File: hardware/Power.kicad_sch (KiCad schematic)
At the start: 22 parts, among them J1 BarrelJack, Q1 DMP3099L-7, U1 ADP7142AUJZ-3.3, U2 ADP7142AUJZ-5.0, U3 ADP7142AUJZ-2.5

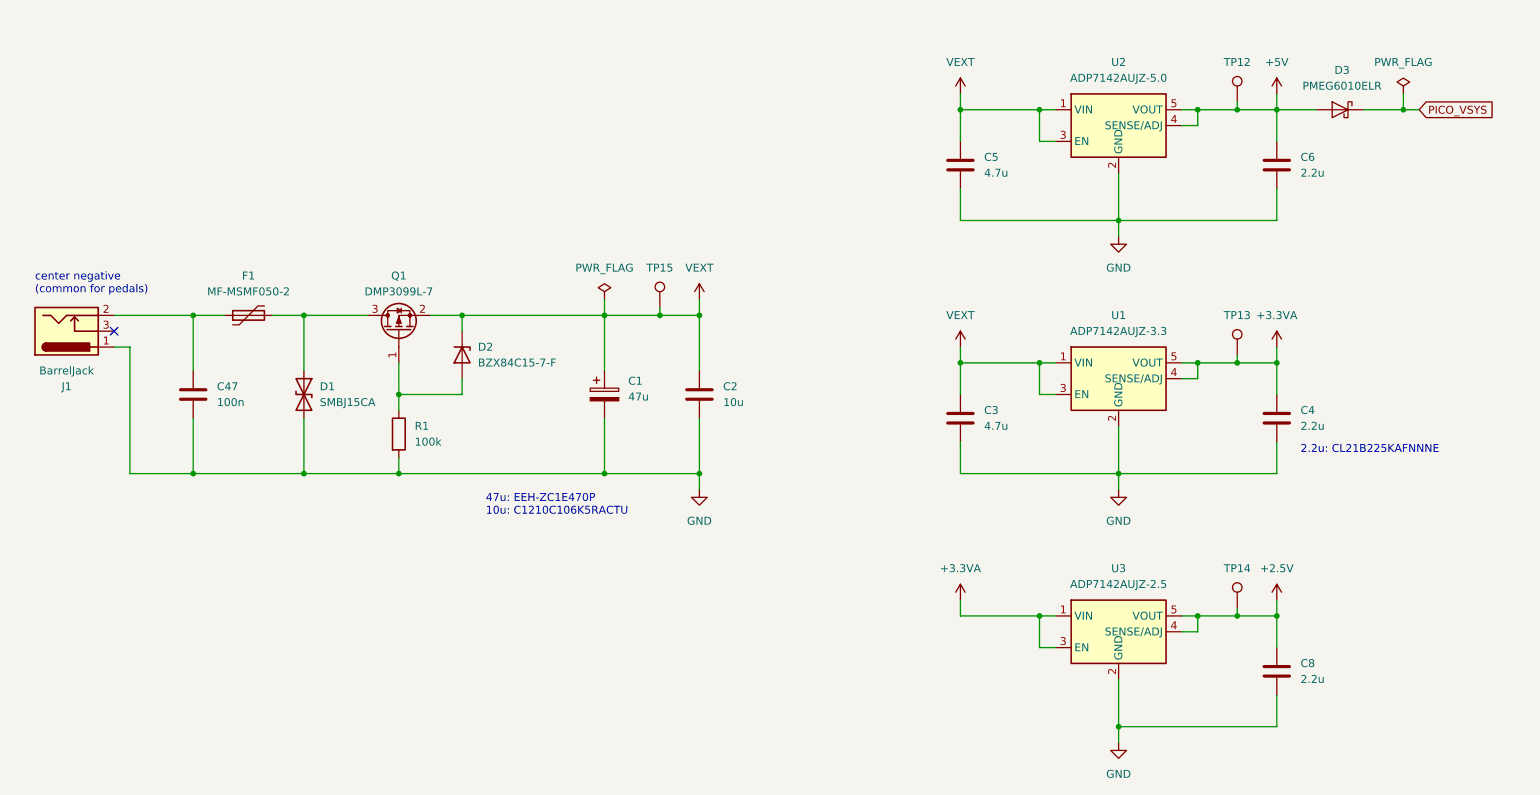
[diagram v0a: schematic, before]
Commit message: final board, pinouts unchecked
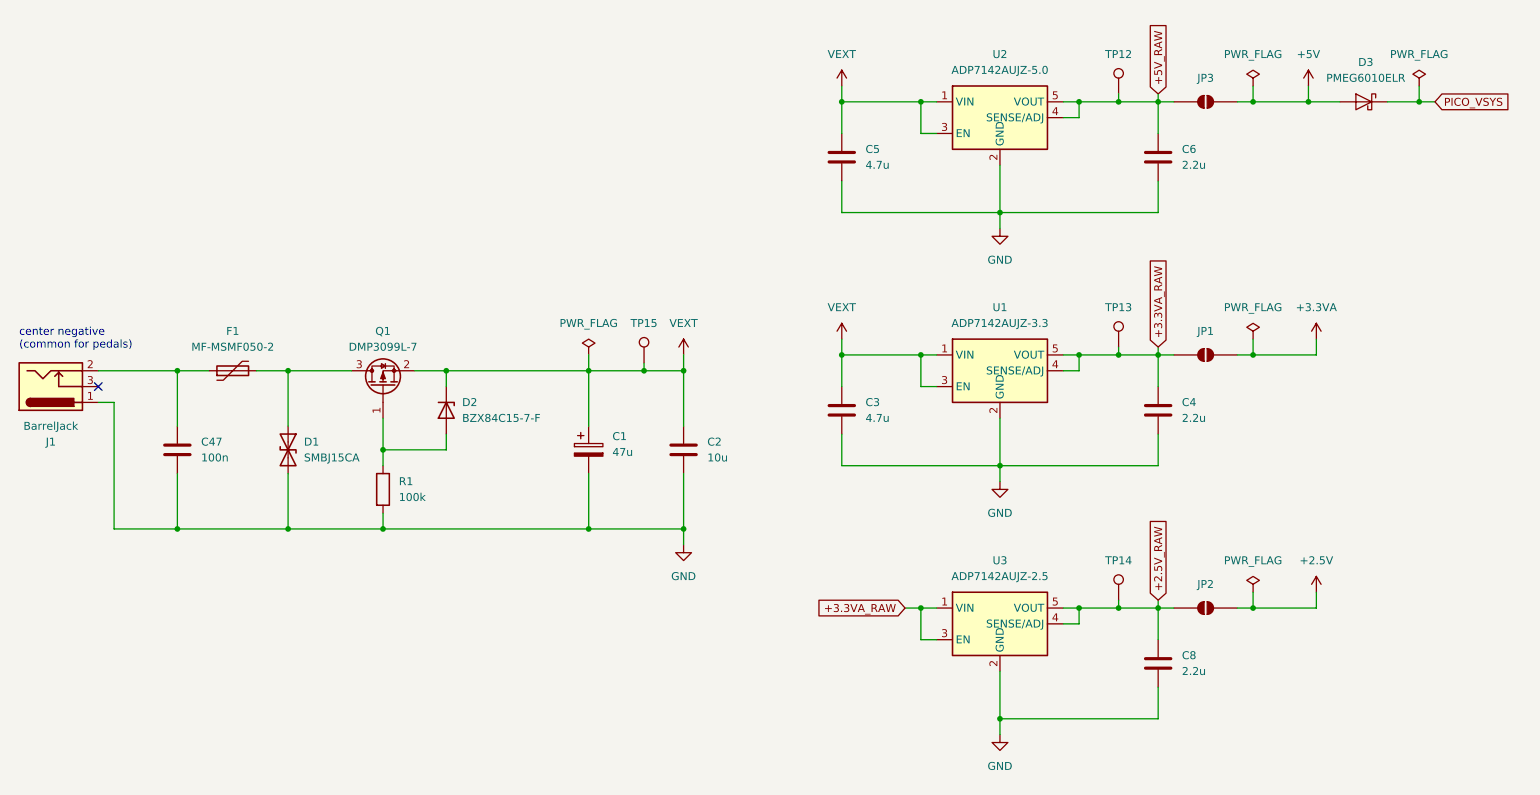
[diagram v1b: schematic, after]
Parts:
- added JP1, JP2, JP3: SolderJumper_2_Open, Jumper:SolderJumper-2_P1.3mm_Open_RoundedPad1.0x1.5mm, symbol Jumper:SolderJumper_2_Open
- TP12, TP13, TP14, TP15: Part Source Uni -> -
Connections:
- net +2.5V: now also JP2.2 (B); no longer C8.1, TP14.1, U3.4 (SENSE/ADJ), U3.5 (VOUT)
- net +3.3VA: now also JP1.2 (B); no longer C4.1, TP13.1, U1.4 (SENSE/ADJ), U1.5 (VOUT), U3.1 (VIN), U3.3 (EN)
- net +5V: now also JP3.2 (B); no longer C6.1, TP12.1, U2.4 (SENSE/ADJ), U2.5 (VOUT)
- new net +2.5V_RAW: C8.1, JP2.1 (A), TP14.1, U3.4 (SENSE/ADJ), U3.5 (VOUT)
- new net +3.3VA_RAW: C4.1, JP1.1 (A), TP13.1, U1.4 (SENSE/ADJ), U1.5 (VOUT), U3.1 (VIN), U3.3 (EN)
- new net +5V_RAW: C6.1, JP3.1 (A), TP12.1, U2.4 (SENSE/ADJ), U2.5 (VOUT)
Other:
- note removed: "2.2u: CL21B225KAFNNNE"
- note removed: "47u: EEH-ZC1E470P 10u: C1210C106K5RACTU"
- moved on the sheet: C1, C2, C3, C4, C47, C5, C6, C8, D1, D2, D3, F1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

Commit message: added signed declaration and updated schematic names
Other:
- company: (none) -> Amon Benson, TU Berlin
- title: (none) -> Power
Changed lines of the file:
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@@
 	(generator_version "10.0")
 	(paper "A4")
+	(title_block
+		(title "Power")
+		(date "2026-09-27")
+		(rev "1.0")
+		(company "Amon Benson, TU Berlin")
+	)
 	(text "center negative\n(common for pedals)"
 		(exclude_from_sim no)
